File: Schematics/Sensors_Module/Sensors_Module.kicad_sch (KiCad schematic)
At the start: 109 parts, among them J1 Stack Male Edge Connector, J2 SWD_01x04_Pin, J4 Screw_Terminal_01x02, J4 USB_C_Female_USB2_Small, J5 Screw_Terminal, J6 CAM_PWR, J7 CAM_DAT, Q3 AO3400A, Q3 AO3401A, Q4 AO3400A, SW1 SW_STM_RESET, SW2 SW_STM_BOOT_MODE, U1 CP2102N-Axx-xQFN28, U1 LM66100DCKR, U1 STM32F103CBT6, U10 ACS70331EOLC, U12 AMS1117-3.3, U12 BM1422AGMV, U3 W25Q128JVS, U4 MMC5633NJL, U5 LM66100DCKR, U6 LM66100DCKR, U8 ISO1042BDWVR, U9 BME680, Y1 X322516MMB4SI

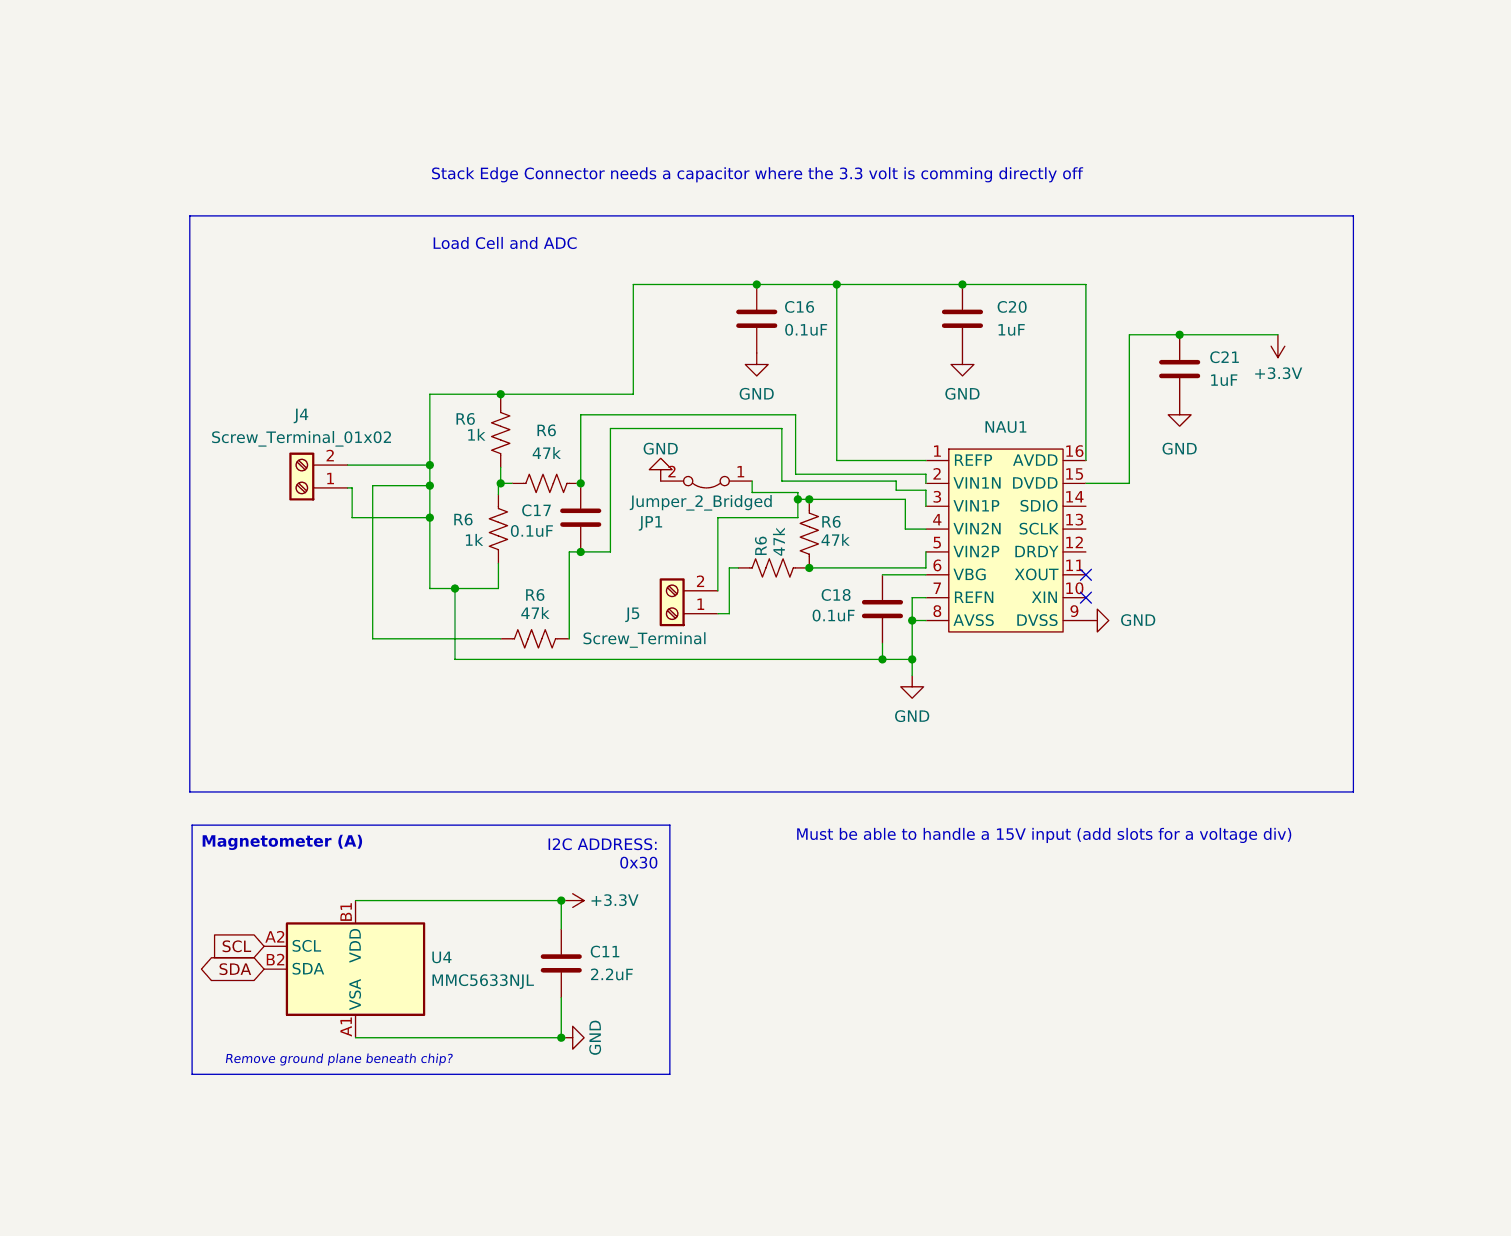
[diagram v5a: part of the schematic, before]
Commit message: Removed load cell ADC & old magnetometer
Screenshot of circuit was left for reference
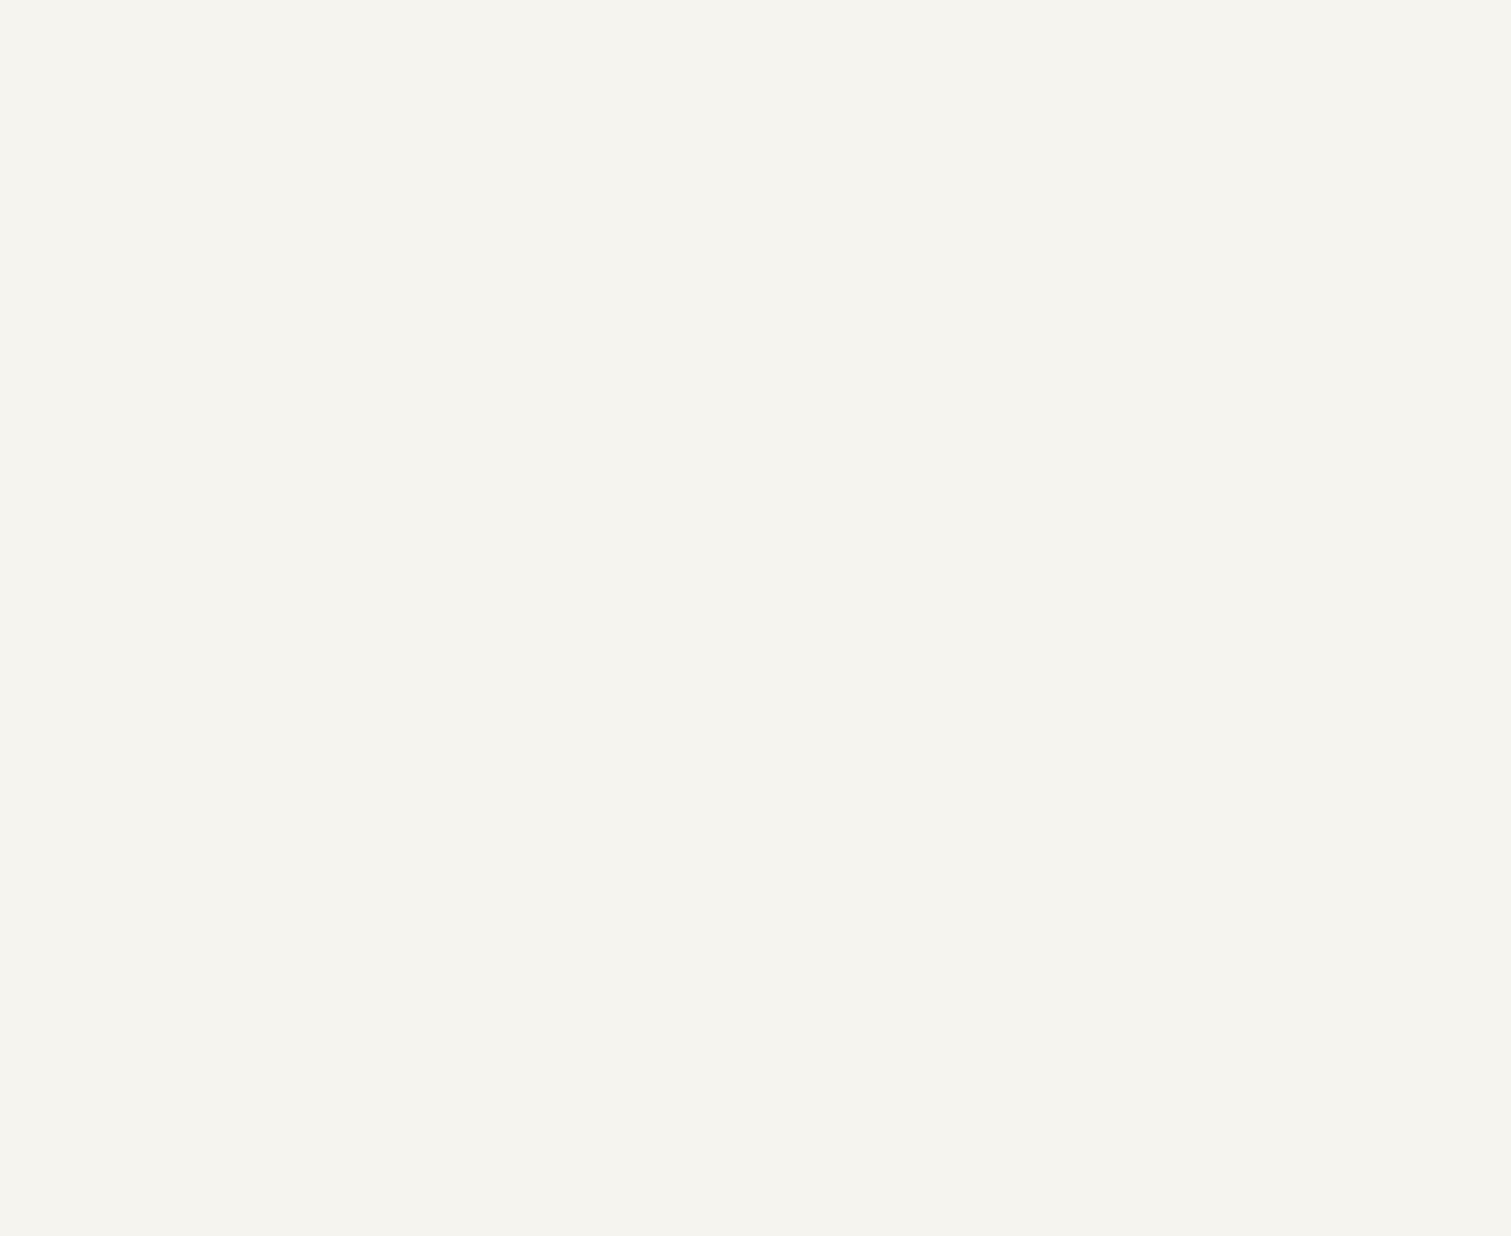
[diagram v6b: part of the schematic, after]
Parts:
- removed C11: 2.2uF, symbol Device:C
- removed C16, C17, C18: 0.1uF, symbol Device:C
- removed C20, C21: 1uF, symbol Device:C
- removed J4: Screw_Terminal_01x02, symbol Connector:Screw_Terminal_01x02
- removed J5: Screw_Terminal, symbol Connector:Screw_Terminal_01x02
- removed JP1: Jumper_2_Bridged, symbol Jumper:Jumper_2_Bridged
- removed NAU1: ~, symbol Libary:NAU7802
- removed R6 (x2): 1k, symbol Device:R_US
- removed R6 (x4): 47k, symbol Device:R_US
- removed U4: MMC5633NJL, Package_BGA:WLP-4_0.86x0.86mm_P0.4mm, symbol Sensor_Magnetic:MMC5633NJL
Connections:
- no-connect marks 34 -> 32
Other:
- note removed: "I2C ADDRESS: 0x30"
- note removed: "Load Cell and ADC"
- note removed: "Magnetometer (A)"
- note removed: "Must be able to handle a 15V input (add slots for a voltage div)"
- note removed: "Stack Edge Connector needs a capacitor where the 3.3 volt is comming directly off"

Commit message: Updated part numbers & footprints + reorganized schematic
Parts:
- added TP13: PB7, TestPoint:TestPoint_Pad_1.5x1.5mm, symbol Connector:TestPoint
- added TP13: PB6, TestPoint:TestPoint_Pad_1.5x1.5mm, symbol Connector:TestPoint
- added TP13: PA0, TestPoint:TestPoint_Pad_1.5x1.5mm, symbol Connector:TestPoint
- added TP14: PA1, TestPoint:TestPoint_Pad_1.5x1.5mm, symbol Connector:TestPoint
- added TP14: PB5, TestPoint:TestPoint_Pad_1.5x1.5mm, symbol Connector:TestPoint
- added TP15: PB4, TestPoint:TestPoint_Pad_1.5x1.5mm, symbol Connector:TestPoint
- C18: footprint Capacitor_SMD:C_0603_1608Metric_Pad1.08x0.95mm_HandSolder -> Capacitor_SMD:C_0603_1608Metric
- C28, C34, C35: footprint (none) -> Capacitor_SMD:C_0603_1608Metric; LCSC (none) -> C15849
- C32, C33: footprint (none) -> Capacitor_SMD:C_0603_1608Metric; LCSC (none) -> C14663
- D2, D4: Digikey (none) -> 1568-COM-16347CT-ND
- J1, TP10, TP2, TP3, TP4, TP5, TP6, TP7, TP8, TP9: now left out of the parts list
- J6: Digikey (none) -> ED10561-ND
- J7: Digikey (none) -> ED10562-ND
- R5: LCSC (none) -> C22978
- R7: value 560R -> 680R; LCSC C23204 -> C23228
- TP13: value TP_PA5 -> PA4
- TP14: value TP_PA6 -> PA5
- TP15: value TP_PA7 -> PA6
- U1, U5, U6: footprint DCK6_TEX -> LMR66100:SC-70-6_Handsoldering; Digikey 296-53541-1-ND -> (none); LCSC (none) -> C2869734
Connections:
- net at U1.10 (PA0): now also TP13.1
- net at U1.11 (PA1): now also TP14.1
- net at U1.40 (PB4): now also TP15.1
- net at U1.41 (PB5): now also TP14.1
- net at U1.42 (PB6): now also TP13.1
- net at U1.43 (PB7): now also TP13.1
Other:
- note added: "Vf=2.1V, I=1.8mA, R=680"
- note removed: "Vf=2.3V, I=1.8mA, R=560"
- moved on the sheet: C10, C28, C3, C30, C32, C33, C34, C35, C7, J6, J7, Q3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

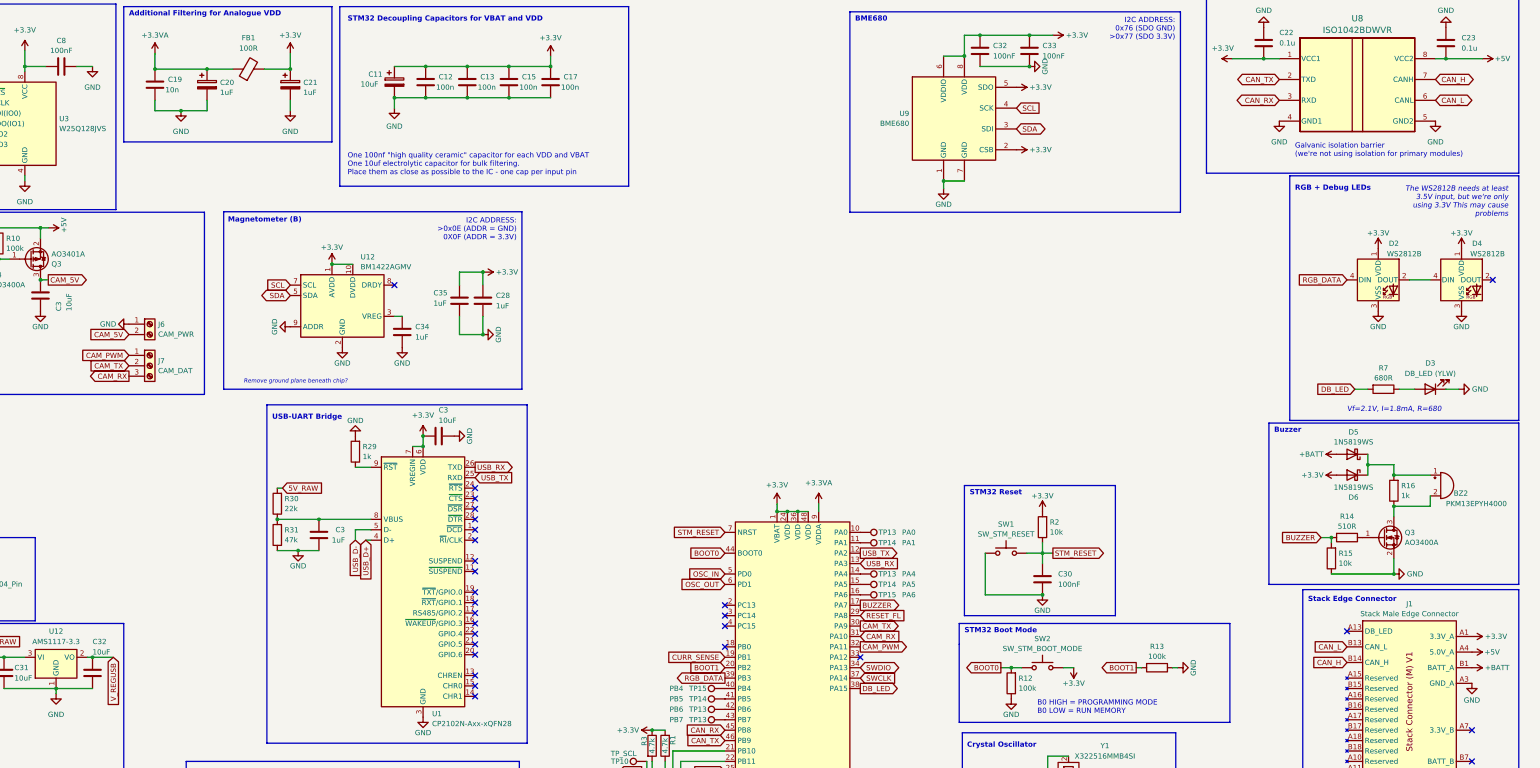
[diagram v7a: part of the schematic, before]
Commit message: Completed PCB layout
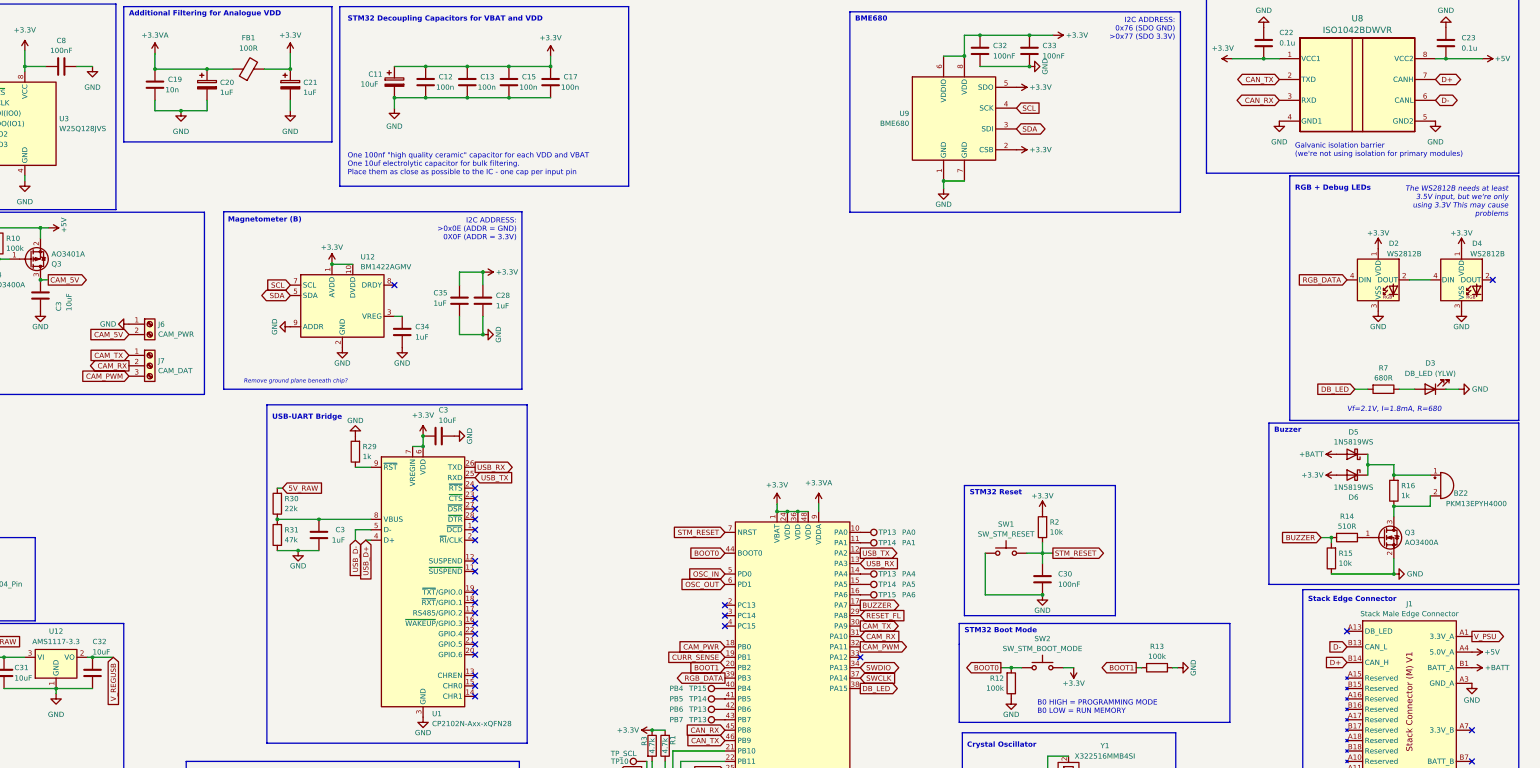
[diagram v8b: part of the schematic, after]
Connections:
- net +3.3V: no longer J1.A1 (3.3V_A), J1.A2 (3.3V_A)
- net CAM_PWM: now also J7.3 (Pin_3); no longer J7.1 (Pin_1)
- net CAM_PWR: now also U1.18 (PB0)
- net CAM_RX: now also J7.2 (Pin_2); no longer J7.3 (Pin_3)
- net CAM_TX: now also J7.1 (Pin_1); no longer J7.2 (Pin_2)
- net V_PSU: now also J1.A1 (3.3V_A), J1.A2 (3.3V_A)
- net CAN_H renamed D+
- net CAN_L renamed D-
- no-connect marks 32 -> 31
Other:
- moved on the sheet: R12
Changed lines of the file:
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@@
   (no_connect (at 164.465 153.035))
   (no_connect (at 144.78 85.725))
-  (no_connect (at 225.425 173.99))
   (no_connect (at 36.83 198.12))
   (no_connect (at 164.465 155.575))
@@
     )
   )
-  (global_label "CAM_PWM" (shape input) (at 80.01 102.87 180) (fields_autoplaced)
+  (global_label "CAM_PWM" (shape input) (at 80.01 107.95 180) (fields_autoplaced)
     (effects (font (size 1.27 1.27)) (justify right))
-    (property "Intersheetrefs" "${INTERSHEET_REFS}" (at 68.0744 102.87 0)
+    (property "Intersheetrefs" "${INTERSHEET_REFS}" (at 68.0744 107.95 0)
       (effects (font (size 1.27 1.27)) (justify right) hide)
     )
@@
     )
   )
+  (global_label "CAM_PWR" (shape input) (at 225.425 173.99 180) (fields_autoplaced)
+    (effects (font (size 1.27 1.27)) (justify right))
+    (property "Intersheetrefs" "${INTERSHEET_REFS}" (at 213.6708 173.99 0)
+      (effects (font (size 1.27 1.27)) (justify right) hide)
+    )
+  )
   (global_label "MOSI_FL" (shape input) (at 44.45 43.815 180) (fields_autoplaced)
     (effects (font (size 1.27 1.27)) (justify right))
@@
     )
   )
-  (global_label "CAN_H" (shape bidirectional) (at 398.78 35.56 0) (fields_autoplaced)
+  (global_label "D+" (shape bidirectional) (at 398.78 35.56 0) (fields_autoplaced)
     (effects (font (size 1.27 1.27)) (justify left))
-    (property "Intersheetrefs" "${INTERSHEET_REFS}" (at 408.8637 35.56 0)
+    (property "Intersheetrefs" "${INTERSHEET_REFS}" (at 405.7189 35.56 0)
       (effects (font (size 1.27 1.27)) (justify left) hide)
     )
@@
     )
   )
-  (global_label "CAN_L" (shape bidirectional) (at 398.78 40.64 0) (fields_autoplaced)
+  (global_label "D-" (shape bidirectional) (at 398.78 40.64 0) (fields_autoplaced)
     (effects (font (size 1.27 1.27)) (justify left))
-    (property "Intersheetrefs" "${INTERSHEET_REFS}" (at 408.5613 40.64 0)
+    (property "Intersheetrefs" "${INTERSHEET_REFS}" (at 405.7189 40.64 0)
       (effects (font (size 1.27 1.27)) (justify left) hide)
     )
@@
     )
   )
-  (global_label "CAN_H" (shape input) (at 377.19 177.8 180) (fields_autoplaced)
+  (global_label "D+" (shape input) (at 377.19 177.8 180) (fields_autoplaced)
     (effects (font (size 1.27 1.27)) (justify right))
-    (property "Intersheetrefs" "${INTERSHEET_REFS}" (at 368.2176 177.8 0)
+    (property "Intersheetrefs" "${INTERSHEET_REFS}" (at 371.3624 177.8 0)
       (effects (font (size 1.27 1.27)) (justify right) hide)
     )
@@
     )
   )
-  (global_label "CAM_RX" (shape output) (at 80.01 107.95 180) (fields_autoplaced)
+  (global_label "CAM_RX" (shape output) (at 80.01 105.41 180) (fields_autoplaced)
     (effects (font (size 1.27 1.27)) (justify right))
-    (property "Intersheetrefs" "${INTERSHEET_REFS}" (at 69.7677 107.95 0)
+    (property "Intersheetrefs" "${INTERSHEET_REFS}" (at 69.7677 105.41 0)
       (effects (font (size 1.27 1.27)) (justify right) hide)
     )
@@
     )
   )
-  (global_label "CAM_TX" (shape input) (at 80.01 105.41 180) (fields_autoplaced)
+  (global_label "CAM_TX" (shape input) (at 80.01 102.87 180) (fields_autoplaced)
     (effects (font (size 1.27 1.27)) (justify right))
-    (property "Intersheetrefs" "${INTERSHEET_REFS}" (at 70.0701 105.41 0)
+    (property "Intersheetrefs" "${INTERSHEET_REFS}" (at 70.0701 102.87 0)
       (effects (font (size 1.27 1.27)) (justify right) hide)
     )
@@
     )
   )
-  (global_label "CAN_L" (shape input) (at 377.19 173.99 180) (fields_autoplaced)
+  (global_label "D-" (shape input) (at 377.19 173.99 180) (fields_autoplaced)
     (effects (font (size 1.27 1.27)) (justify right))
-    (property "Intersheetrefs" "${INTERSHEET_REFS}" (at 368.52 173.99 0)
+    (property "Intersheetrefs" "${INTERSHEET_REFS}" (at 371.3624 173.99 0)
       (effects (font (size 1.27 1.27)) (justify right) hide)
     )
   )
+  (global_label "V_PSU" (shape output) (at 407.67 171.45 0) (fields_autoplaced)
+    (effects (font (size 1.27 1.27)) (justify left))
+    (property "Intersheetrefs" "${INTERSHEET_REFS}" (at 416.5214 171.45 0)
+      (effects (font (size 1.27 1.27)) (justify left) hide)
+    )
+  )
   (global_label "BOOT1" (shape input) (at 225.425 179.07 180) (fields_autoplaced)
     (effects (font (size 1.27 1.27)) (justify right))
@@
     )
   )
-  (symbol (lib_id "Device:R") (at 295.275 182.88 180) (unit 1)
-    (in_bom yes) (on_board yes) (dnp no) (fields_autoplaced)
-    (property "Reference" "R12" (at 297.053 181.6679 0)
+  (symbol (lib_id "Device:R") (at 295.275 182.88 0) (mirror x) (unit 1)
+    (in_bom yes) (on_board yes) (dnp no)
+    (property "Reference" "R12" (at 293.497 181.6679 0)
       (effects (font (size 1.27 1.27)) (justify right))
     )
-    (property "Value" "100k" (at 297.053 184.0921 0)
+    (property "Value" "100k" (at 293.497 184.0921 0)
       (effects (font (size 1.27 1.27)) (justify right))
     )
-    (property "Footprint" "Resistor_SMD:R_0603_1608Metric" (at 297.053 182.88 90)
+    (property "Footprint" "Resistor_SMD:R_0603_1608Metric" (at 293.497 182.88 90)
       (effects (font (size 1.27 1.27)) hide)
     )
@@
         )
       )
-    )
-  )
-  (symbol (lib_id "power:+3.3V") (at 407.67 171.45 270) (unit 1)
-    (in_bom yes) (on_board yes) (dnp no) (fields_autoplaced)
-    (property "Reference" "#PWR037" (at 403.86 171.45 0)
-      (effects (font (size 1.27 1.27)) hide)
-    )
-    (property "Value" "+3.3V" (at 410.845 171.45 90)
-      (effects (font (size 1.27 1.27)) (justify left))
-    )
-    (property "Footprint" "" (at 407.67 171.45 0)
-      (effects (font (size 1.27 1.27)) hide)
-    )
-    (property "Datasheet" "" (at 407.67 171.45 0)
-      (effects (font (size 1.27 1.27)) hide)
-    )
-    (pin "1")
-    (instances
-      (project "Altimeter_Module"
-        (path "/29db4100-776d-46b8-a17b-170206e82f23"
-          (reference "#PWR037") (unit 1)
-        )
-      )
-      (project "Communications_Module"
-        (path "/ace06731-9b48-45c3-868d-c65fed1a8f9b"
-          (reference "#PWR05") (unit 1)
-        )
-      )
-      (project "Sensors_Module"
-        (path "/e77d0584-110f-4b35-98c2-0ebac97a828e"
-          (reference "#PWR035") (unit 1)
-        )
-      )
